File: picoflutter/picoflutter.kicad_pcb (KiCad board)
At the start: 4 copper layers, 70.5 x 55 mm, 67 parts, among them IC1 AP7361EA-33E-13, IC3 W25Q64JVZPIQ, J2 SM04B-SRSS-TB, J4 S2B-PH-SM4-TB(LF)(SN), J5 USB4105-GF-A, Q1 DMG3415, SW2 MK-12C02-G020, U1 MCP73831T-2ACI/OT, U3 RP2040, Y1 445I23D12M00000

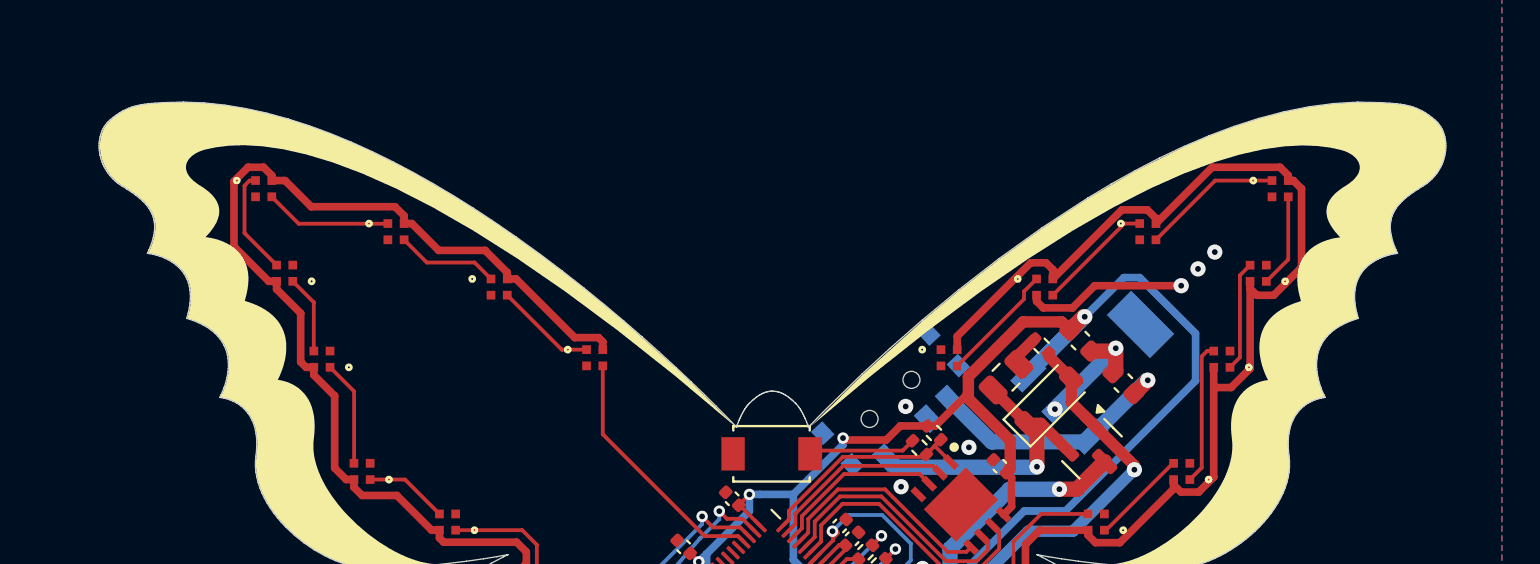
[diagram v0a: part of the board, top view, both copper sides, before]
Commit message: fixed leds power supply
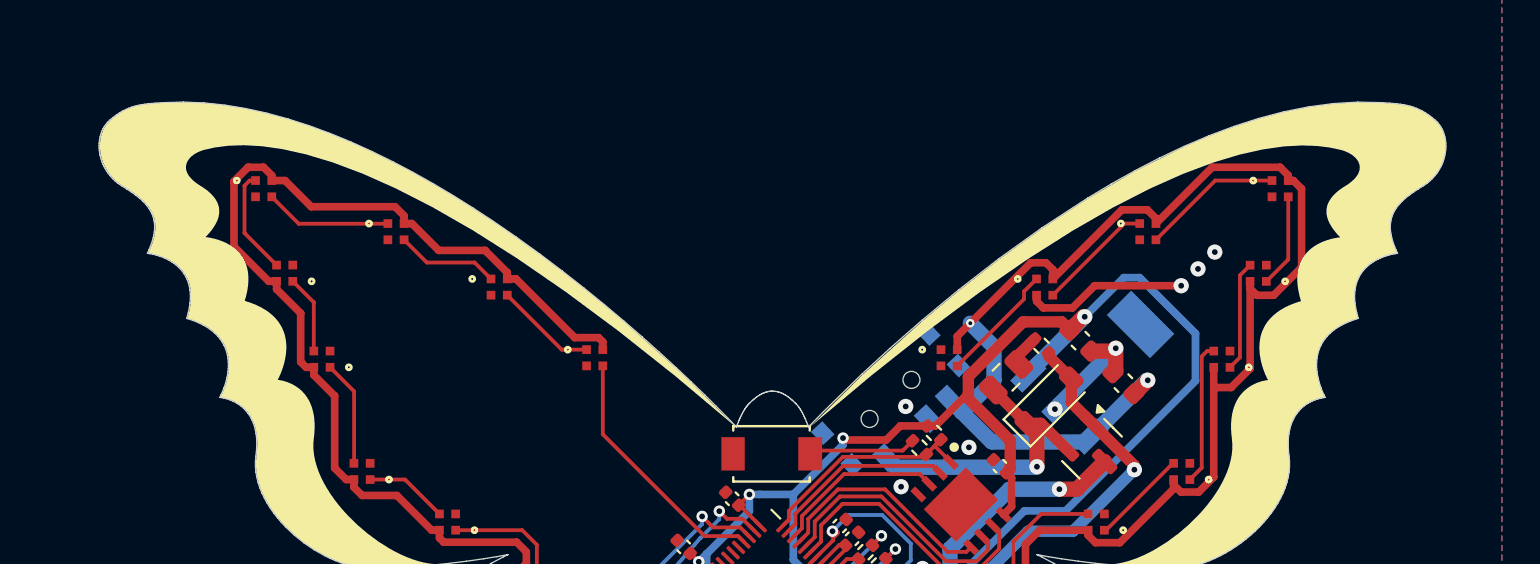
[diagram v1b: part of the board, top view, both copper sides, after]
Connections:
- C1 pad 1: Net-(IC1-IN) -> +5V
- IC1 pad 1: Net-(IC1-IN) -> +5V
- SW2 pad 3: Net-(IC1-IN) -> +5V
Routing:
- net +5V: track 233.1 -> 252.6 mm, vias 5 -> 7
- net Net-(IC1-IN): track 13.7 -> 0.00 mm, vias 1 -> 0
- net (no net): vias 2 -> 0
